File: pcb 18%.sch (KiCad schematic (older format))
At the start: 1 part

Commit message: part 3 finish. Schematic things around the mcu
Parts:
- added C?: 1uF, symbol Device:C_Small
- added C? (x3): 0.1uF, symbol Device:C_Small
- added C?: 10uF, symbol Device:C_Small
- added C? (x2): 22pF, symbol Device:C_Small
- added R: 10k, symbol Device:R_Small
- added R? (x2): 22, symbol Device:R_Small
- added R?: R_Small, symbol Device:R_Small
- added SW?: SW_Push, symbol Switch:SW_Push
- added Y?: 16MHz, symbol Device:Crystal_GND24_Small
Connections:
- net at U?.13 (~RESET): now also R?.2, SW?.2
- net +5V: now reaches U?.14 (VCC), U?.34 (VCC)
- net +5V: now also U?.2 (UVCC), U?.24 (AVCC), U?.44 (AVCC), U?.7 (VBUS), C?.1, C?.1, C?.1, C?.1, R?.1
- net GND: now reaches U?.15 (GND), U?.23 (GND), U?.35 (GND), U?.43 (GND)
- net GND: now also U?.5 (UGND), C?.2, C?.2, C?.2, C?.2, C?.2, C?.2, C?.2, R.1, SW?.1, Y?.2, Y?.4
- net at U?.16 (XTAL2): now also C?.1, Y?.1
- net at U?.17 (XTAL1): now also C?.1, Y?.3
- net at U?.3 (D-): now also R?.1
- net at U?.33 (~HWB~/PE2): now also R.2
- net at U?.4 (D+): now also R?.1
- net at U?.6 (UCAP): now also C?.1
- new net D+: R?.2
- new net D-: R?.2

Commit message: switch matrix anfänge
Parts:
- removed U?: ATmega32U4-AU, Package_QFP:TQFP-44_10x10mm_P0.8mm, symbol MCU_Microchip_ATmega:ATmega32U4-AU
- removed Y?: 16MHz, symbol Device:Crystal_GND24_Small
- added D? (x8): D_Small, symbol Device:D_Small
- added MX? (x8): MX-NoLED, symbol MX_Alps_Hybrid:MX-NoLED
- added U?: ATmega32U4-AU, Package_QFP:TQFP-44_10x10mm_P0.8mm, symbol MCU_Microchip_ATmega:ATmega32U4-AU
- added Y?: 16MHz, symbol Device:Crystal_GND24_Small
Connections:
- net +5V: now also U?.14 (VCC), U?.2 (UVCC), U?.34 (VCC), U?.7 (VBUS)
- net GND: now also SW?.2, U?.15 (GND), U?.23 (GND), U?.35 (GND), U?.43 (GND), U?.5 (UGND), Y?.2, Y?.4; no longer SW?.1
- net at R?.2: now also SW?.1, U?.13 (~RESET); no longer SW?.2
- net at C?.1: now also U?.16 (XTAL2), Y?.3
- net at C?.1: now also U?.17 (XTAL1), Y?.1
- net at R?.1: now also U?.3 (D-)
- net at R.2: now also U?.33 (~HWB~/PE2)
- net at R?.1: now also U?.4 (D+)
- net at C?.1: now also U?.6 (UCAP)
- new net: U?.24 (AVCC), U?.44 (AVCC)
- new net: D?.2 (A), MX?.2 (ROW) (x8)
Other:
- moved on the sheet: C?, R, R?, SW?

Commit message: schematic file finish
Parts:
- removed D? (x6): D_Small, symbol Device:D_Small
- removed MX? (x6): MX-NoLED, symbol MX_Alps_Hybrid:MX-NoLED
- added D3, D4, D5, D6, D7, D8: D_Small, Diode_SMD:D_SOD-123, symbol Device:D_Small
- added F?: Polyfuse_Small, symbol Device:Polyfuse_Small
- added MX3, MX4, MX5, MX6, MX7, MX8: MX-NoLED, MX_Alps_Hybrid:MX-1U-NoLED, symbol MX_Alps_Hybrid:MX-NoLED
- added USB_jst_connector: Conn_01x04, symbol Connector_Generic:Conn_01x04
- C1, C2, C3, C4, C5, C6, C7: renamed from C?; footprint (none) -> Capacitor_SMD:C_0805_2012Metric
- D1, D2: renamed from D?; footprint (none) -> Diode_SMD:D_SOD-123
- MX1, MX2: renamed from MX?; footprint (none) -> MX_Alps_Hybrid:MX-1U-NoLED
- R1, R2, R3: renamed from R?; footprint (none) -> Resistor_SMD:R_0805_2012Metric
- R4: renamed from R; footprint (none) -> Resistor_SMD:R_0805_2012Metric
- SW1: renamed from SW?; footprint (none) -> random-keyboard-parts:SKQG-1155865
- Y1: renamed from Y?; footprint (none) -> Crystal:Crystal_SMD_3225-4Pin_3.2x2.5mm
- gave numbers to parts that had none: 1
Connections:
- net +5V: now also U1.24 (AVCC), U1.44 (AVCC), F?.2
- net D+: now also USB_jst_connector.2 (Pin_2)
- net D-: now also USB_jst_connector.3 (Pin_3)
- net GND: now also USB_jst_connector.4 (Pin_4)
- net COL_0: now reaches MX1.1 (COL)
- net COL_0: now also MX2.1 (COL)
- net ROW_0: now reaches D1.1 (K)
- net ROW_0: now also D3.1 (K), D5.1 (K), D7.1 (K)
- net ROW_1: now reaches D2.1 (K)
- net ROW_1: now also D4.1 (K), D6.1 (K), D8.1 (K)
- new net: F?.1, USB_jst_connector.1 (Pin_1)
- new net: D3.2 (A), MX3.2 (ROW)
- new net: D4.2 (A), MX4.2 (ROW)
- new net: D5.2 (A), MX5.2 (ROW)
- new net: D6.2 (A), MX6.2 (ROW)
- new net: D7.2 (A), MX7.2 (ROW)
- new net: D8.2 (A), MX8.2 (ROW)
- new net COL_1: MX3.1 (COL), MX4.1 (COL)
- new net COL_2: MX5.1 (COL), MX6.1 (COL)
- new net COL_3: MX7.1 (COL), MX8.1 (COL)
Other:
- moved on the sheet: C1, C2, C3, C4, C5, C6, C7, D1, D2, MX1, MX2, R1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

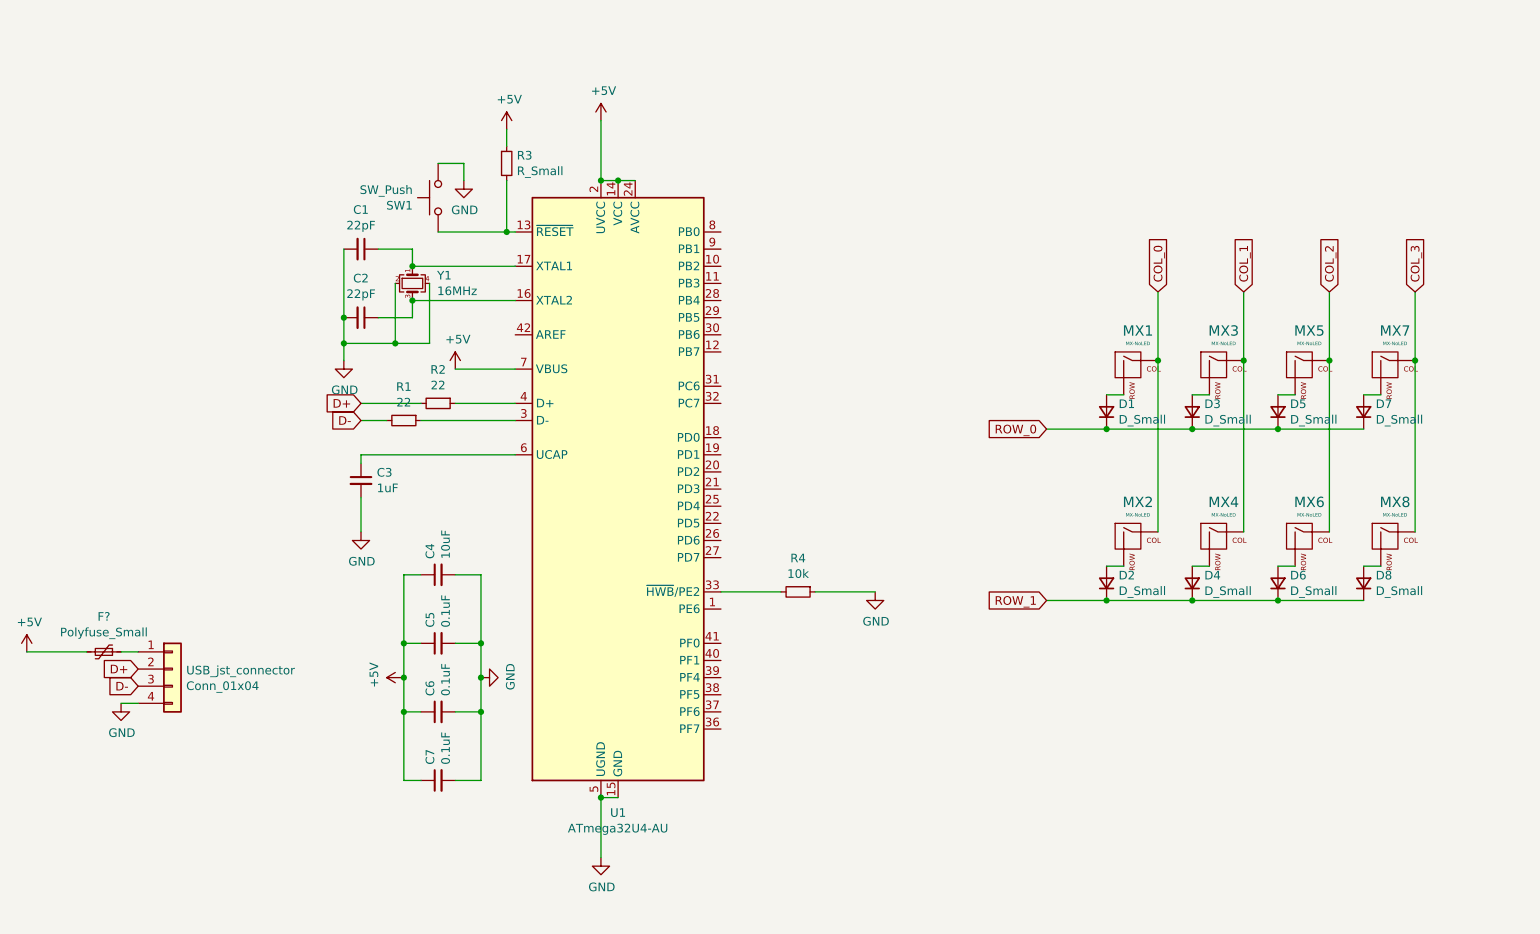
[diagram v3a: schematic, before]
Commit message: poti lib & sch
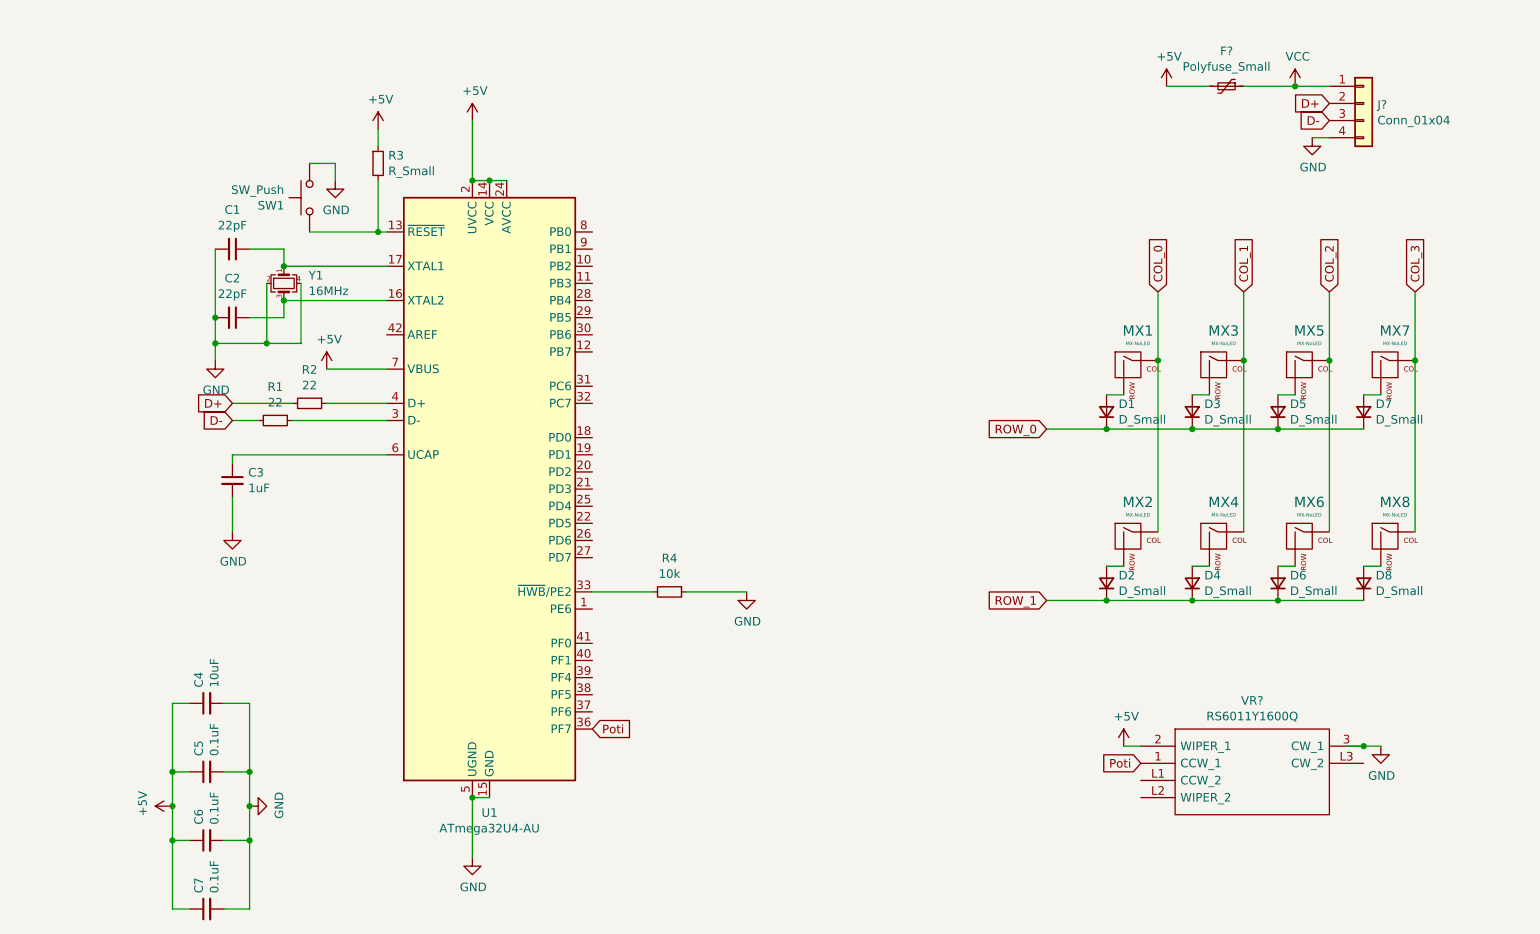
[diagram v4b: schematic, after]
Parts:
- added VR?: RS6011Y1600Q, RS6011Y1600Q, symbol RS6011Y1600Q:RS6011Y1600Q
- renumbered USB_jst_connector to J?
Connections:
- net +5V: now also VR?.2 (WIPER_1)
- net GND: now also VR?.3 (CW_1)
- net VCC: now reaches F?.1, J?.1 (Pin_1)
- net Poti: now reaches U1.36 (PF7)
- net Poti: now also VR?.1 (CCW_1)
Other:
- moved on the sheet: C1, C2, C3, C4, C5, C6, C7, F?, J?, R1, R2, R3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

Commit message: diesdas
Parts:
- added C8: 100nF, Capacitor_SMD:C_0805_2012Metric, symbol Device:C_Small
- added L1: 10μH, symbol Device:L_Small
- J1: renamed from J?; footprint (none) -> random-keyboard-parts:JST-SR-4
- VR1: renamed from VR?; footprint RS6011Y1600Q -> RS6011Y1600Q:RS6011Y1600Q
- gave numbers to parts that had none: 1
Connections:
- net +5V: now also L1.1; no longer U1.24 (AVCC), U1.44 (AVCC), VR1.2 (WIPER_1)
- net COL_0: now also U1.10 (PB2)
- net COL_1: now also U1.11 (PB3)
- net COL_2: now also U1.28 (PB4)
- net COL_3: now also U1.29 (PB5)
- net GND: now also C8.1
- net ROW_0: now also U1.8 (PB0)
- net ROW_1: now also U1.9 (PB1)
- new net Poti_In: C8.2, L1.2, U1.24 (AVCC), U1.44 (AVCC), VR1.2 (WIPER_1)
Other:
- moved on the sheet: D1, D2, D3, D4, D5, D6, D7, D8, F1, J1, MX1, MX2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

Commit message: pcb anfänge
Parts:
- removed C8: 100nF, Capacitor_SMD:C_0805_2012Metric, symbol Device:C_Small
- removed L1: 10μH, symbol Device:L_Small
- removed VR1: RS6011Y1600Q, RS6011Y1600Q:RS6011Y1600Q, symbol RS6011Y1600Q:RS6011Y1600Q
- F1: footprint (none) -> Fuse:Fuse_1206_3216Metric
- J1: footprint random-keyboard-parts:JST-SR-4 -> Connector_JST:JST_SH_SM04B-SRSS-TB_1x04-1MP_P1.00mm_Horizontal
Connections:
- net Poti_In is gone; now on net +5V: U1.24 (AVCC), U1.44 (AVCC)
- net COL_0: no longer U1.10 (PB2)
- net COL_1: no longer U1.11 (PB3)
- net COL_2: no longer U1.28 (PB4)
- net COL_3: no longer U1.29 (PB5)
- net GND: now also SW1.1; no longer SW1.2
- net ROW_0: no longer U1.8 (PB0)
- net ROW_1: no longer U1.9 (PB1)
- net at R3.2, U1.13 (~RESET): now also SW1.2; no longer SW1.1
- net Poti: no longer names the net of U1.36 (PF7)
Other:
- moved on the sheet: C3, D1, D2, D3, D4, D5, D6, D7, D8, F1, J1, MX1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
